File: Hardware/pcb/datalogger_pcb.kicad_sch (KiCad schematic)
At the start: 50 parts, among them J1 Micro_SD_Card_Det2, J2 Switch OUT, SW1 SW_Wuerth_450301014042, SW2 SW_Push, U1 DS3231MZ, U2 SN74LVC2G00DCTR

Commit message: Corrected errors in PCB
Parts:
- added RpullupCS1: 10k, Resistor_SMD:R_0805_2012Metric_Pad1.20x1.40mm_HandSolder, symbol Device:R
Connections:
- net +3.3V: now also RpullupCS1.1
- net CS: now also RpullupCS1.2
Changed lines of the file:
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@@
 	)
 	(junction
+		(at 218.44 142.24)
+		(diameter 0)
+		(color 0 0 0 0)
+	)
+	(junction
 		(at 229.87 36.83)
 		(diameter 0)
@@
 	(wire
 		(pts
-			(xy 226.06 142.24) (xy 237.49 142.24)
+			(xy 210.82 142.24) (xy 218.44 142.24)
 		)
 		(stroke
@@
 	(wire
 		(pts
+			(xy 218.44 142.24) (xy 237.49 142.24)
+		)
+		(stroke
+			(width 0)
+			(type default)
+		)
+	)
+	(wire
+		(pts
 			(xy 224.79 100.33) (xy 224.79 105.41)
 		)
@@
 	(wire
 		(pts
+			(xy 218.44 132.08) (xy 218.44 133.35)
+		)
+		(stroke
+			(width 0)
+			(type default)
+		)
+	)
+	(wire
+		(pts
 			(xy 163.83 82.55) (xy 185.42 82.55)
 		)
@@
 	(wire
 		(pts
+			(xy 218.44 140.97) (xy 218.44 142.24)
+		)
+		(stroke
+			(width 0)
+			(type default)
+		)
+	)
+	(wire
+		(pts
 			(xy 226.06 162.56) (xy 232.41 162.56)
 		)
@@
 	)
 	(label "CS"
-		(at 226.06 142.24 0)
+		(at 210.82 142.24 0)
 		(effects
 			(font
@@
 		(on_board yes)
 		(dnp no)
-		(fields_autoplaced yes)
 		(property "Reference" "#PWR02"
 			(at 220.98 151.13 0)
@@
 		)
 		(property "Value" "+3.3V"
-			(at 220.98 142.24 0)
+			(at 216.916 146.304 0)
 			(effects
 				(font
@@
 	)
 	(symbol
+		(lib_id "Device:R")
+		(at 218.44 137.16 0)
+		(unit 1)
+		(exclude_from_sim no)
+		(in_bom yes)
+		(on_board yes)
+		(dnp no)
+		(fields_autoplaced yes)
+		(property "Reference" "RpullupCS1"
+			(at 220.98 135.8899 0)
+			(effects
+				(font
+					(size 1.27 1.27)
+				)
+				(justify left)
+			)
+		)
+		(property "Value" "10k"
+			(at 220.98 138.4299 0)
+			(effects
+				(font
+					(size 1.27 1.27)
+				)
+				(justify left)
+			)
+		)
+		(property "Footprint" "Resistor_SMD:R_0805_2012Metric_Pad1.20x1.40mm_HandSolder"
+			(at 216.662 137.16 90)
+			(effects
+				(font
+					(size 1.27 1.27)
+				)
+				(hide yes)
+			)
+		)
+		(property "Datasheet" "~"
+			(at 218.44 137.16 0)
+			(effects
+				(font
+					(size 1.27 1.27)
+				)
+				(hide yes)
+			)
+		)
+		(property "Description" "Resistor"
+			(at 218.44 137.16 0)
+			(effects
+				(font
+					(size 1.27 1.27)
+				)
+				(hide yes)
+			)
+		)
+		(pin "1"
+		)
+		(pin "2"
+		)
+		(instances
+			(project "datalogger_pcb"
+				(path "/0cb0c659-ad14-4dc3-8b7e-e8b9c3c06858"
+					(reference "RpullupCS1")
+					(unit 1)
+				)
+			)
+		)
+	)
+	(symbol
 		(lib_id "power:+3.3V")
 		(at 76.2 151.13 0)
@@
 					(unit 1)
 				)
+			)
+		)
+	)
+	(symbol
+		(lib_id "power:+3.3V")
+		(at 218.44 132.08 0)
+		(unit 1)
+		(exclude_from_sim no)
+		(in_bom yes)
+		(on_board yes)
+		(dnp no)
+		(property "Reference" "#PWR024"
+			(at 218.44 135.89 0)
+			(effects
+				(font
+					(size 1.27 1.27)
+				)
+				(hide yes)
+			)
+		)
+		(property "Value" "+3.3V"
+			(at 222.504 130.556 0)
+			(effects
+				(font
+					(size 1.27 1.27)
+				)
+			)
+		)
+		(property "Footprint" ""
+			(at 218.44 132.08 0)
+			(effects
+				(font
+					(size 1.27 1.27)
+				)
+				(hide yes)
+			)
+		)
+		(property "Datasheet" ""
+			(at 218.44 132.08 0)
+			(effects
+				(font
+					(size 1.27 1.27)
+				)
+				(hide yes)
+			)
+		)
+		(property "Description" "Power symbol creates a global label with name \"+3.3V\""
+			(at 218.44 132.08 0)
+			(effects
+				(font
+					(size 1.27 1.27)
+				)
+				(hide yes)
+			)
+		)
+		(pin "1"
+		)
+		(instances
+			(project "datalogger_pcb"
+				(path "/0cb0c659-ad14-4dc3-8b7e-e8b9c3c06858"
+					(reference "#PWR024")
+					(unit 1)
+				)

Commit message: Improvements to PCB
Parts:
- removed MOSFET_12V1, MOSFET_5V1: BS170, Package_TO_SOT_THT:TO-92_Inline, symbol Transistor_FET:BS170
- removed R8: 100, Resistor_SMD:R_0805_2012Metric_Pad1.20x1.40mm_HandSolder, symbol Device:R
- removed R_pdown_MFET_1, R_pdown_MFET_2: 10k, Resistor_SMD:R_0805_2012Metric_Pad1.20x1.40mm_HandSolder, symbol Device:R
- added 12VSWTCH1, 5VSWTCH1: TPS22810DBV, Package_TO_SOT_SMD:SOT-23-6, symbol Power_Management:TPS22810DBV
- added C5, C6: 1uF, Capacitor_SMD:C_1812_4532Metric_Pad1.57x3.40mm_HandSolder, symbol Device:C
- added R6: 10k, Resistor_SMD:R_0805_2012Metric_Pad1.20x1.40mm_HandSolder, symbol Device:R
- R7: value 100 -> 10k
- R_BYPASS1: footprint Resistor_THT:R_Axial_DIN0204_L3.6mm_D1.6mm_P5.08mm_Vertical -> Resistor_SMD:R_0805_2012Metric_Pad1.20x1.40mm_HandSolder
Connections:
- net +12V: now also 12VSWTCH1.1 (VIN), C5.2
- net +5V: now also P_MOSFET1.3 (D), U2.8 (VCC)
- net +5VP: now also R_BYPASS1.2, 5VSWTCH1.1 (VIN), C6.2
- net GND: now also R7.2, 12VSWTCH1.2 (GND), 5VSWTCH1.2 (GND), C5.1, C6.1, R6.2
- net at J2.1 (Pin_1): now also 12VSWTCH1.5 (QOD), 12VSWTCH1.6 (VOUT)
- net at J2.2 (Pin_2): now also 5VSWTCH1.5 (QOD), 5VSWTCH1.6 (VOUT)
- net at A1.34 (GPIO28_ADC2), R7.1: now also 12VSWTCH1.3 (EN/UVLO)
- net at A1.19 (GPIO14), GPIO14-1.2 (Pin_2): now also 5VSWTCH1.3 (EN/UVLO), R6.1
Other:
- moved on the sheet: C3, J1, J2, R3, R4, R_BYPASS1, RpullupCS1

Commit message: Small changes
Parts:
- removed RpullupSCL0, RpullupSDA0: 10k, Resistor_THT:R_Axial_DIN0204_L3.6mm_D1.6mm_P5.08mm_Vertical, symbol Device:R

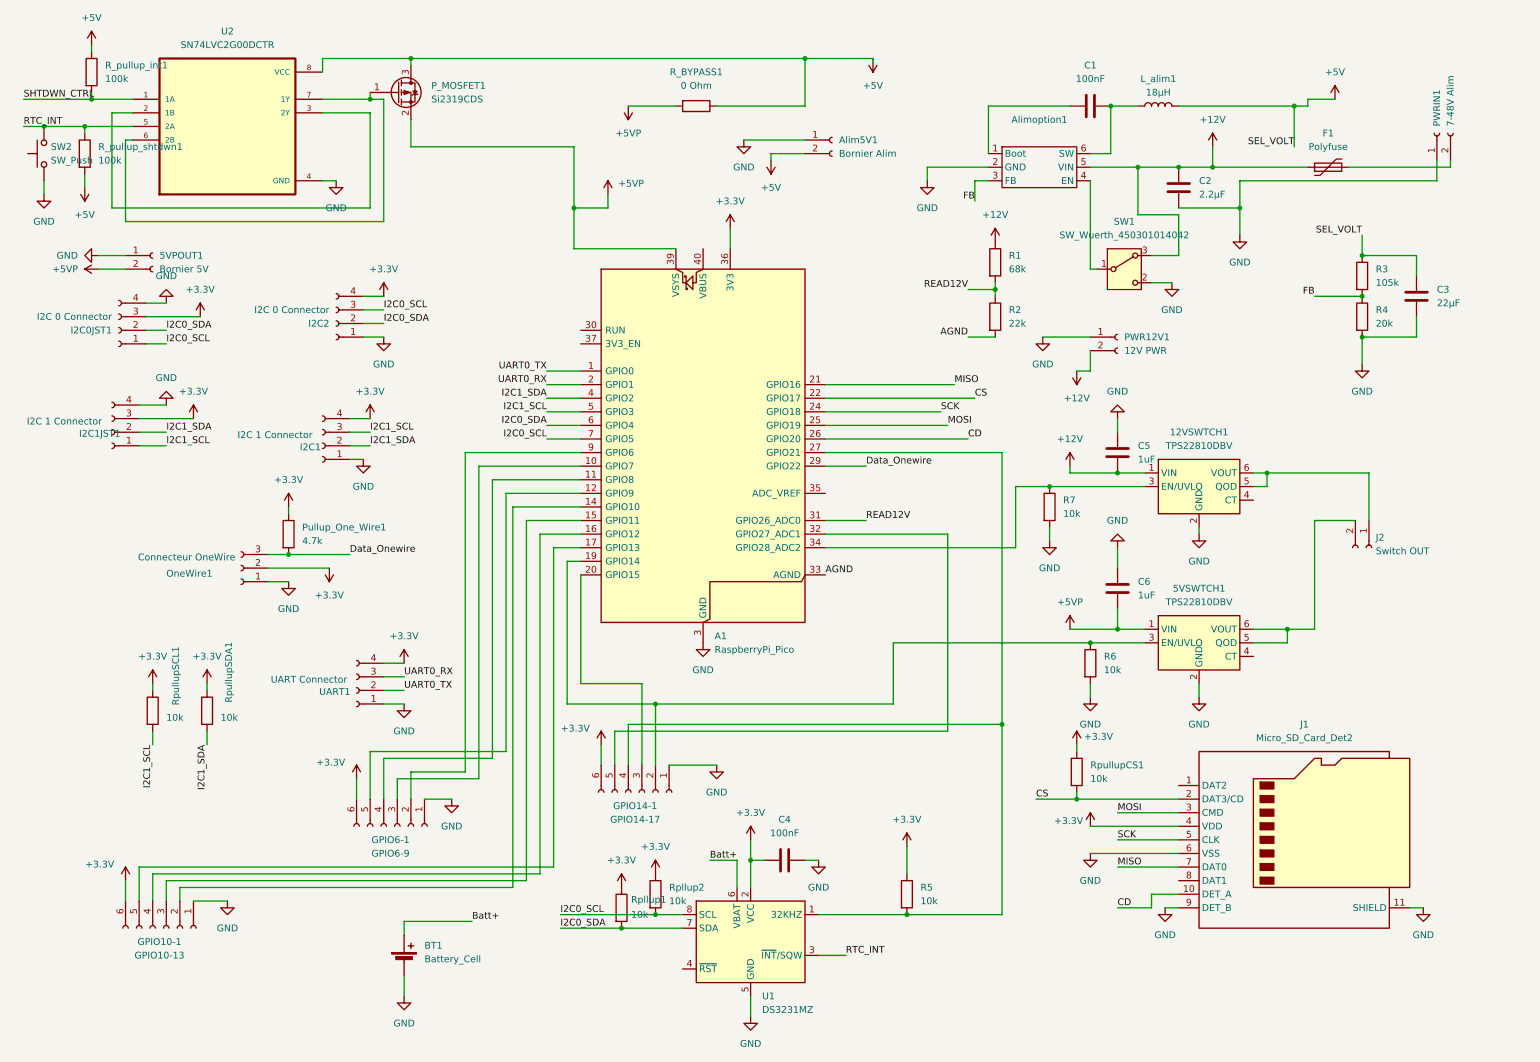
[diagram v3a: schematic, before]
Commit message: Improved datalogger design and reduced pcb size
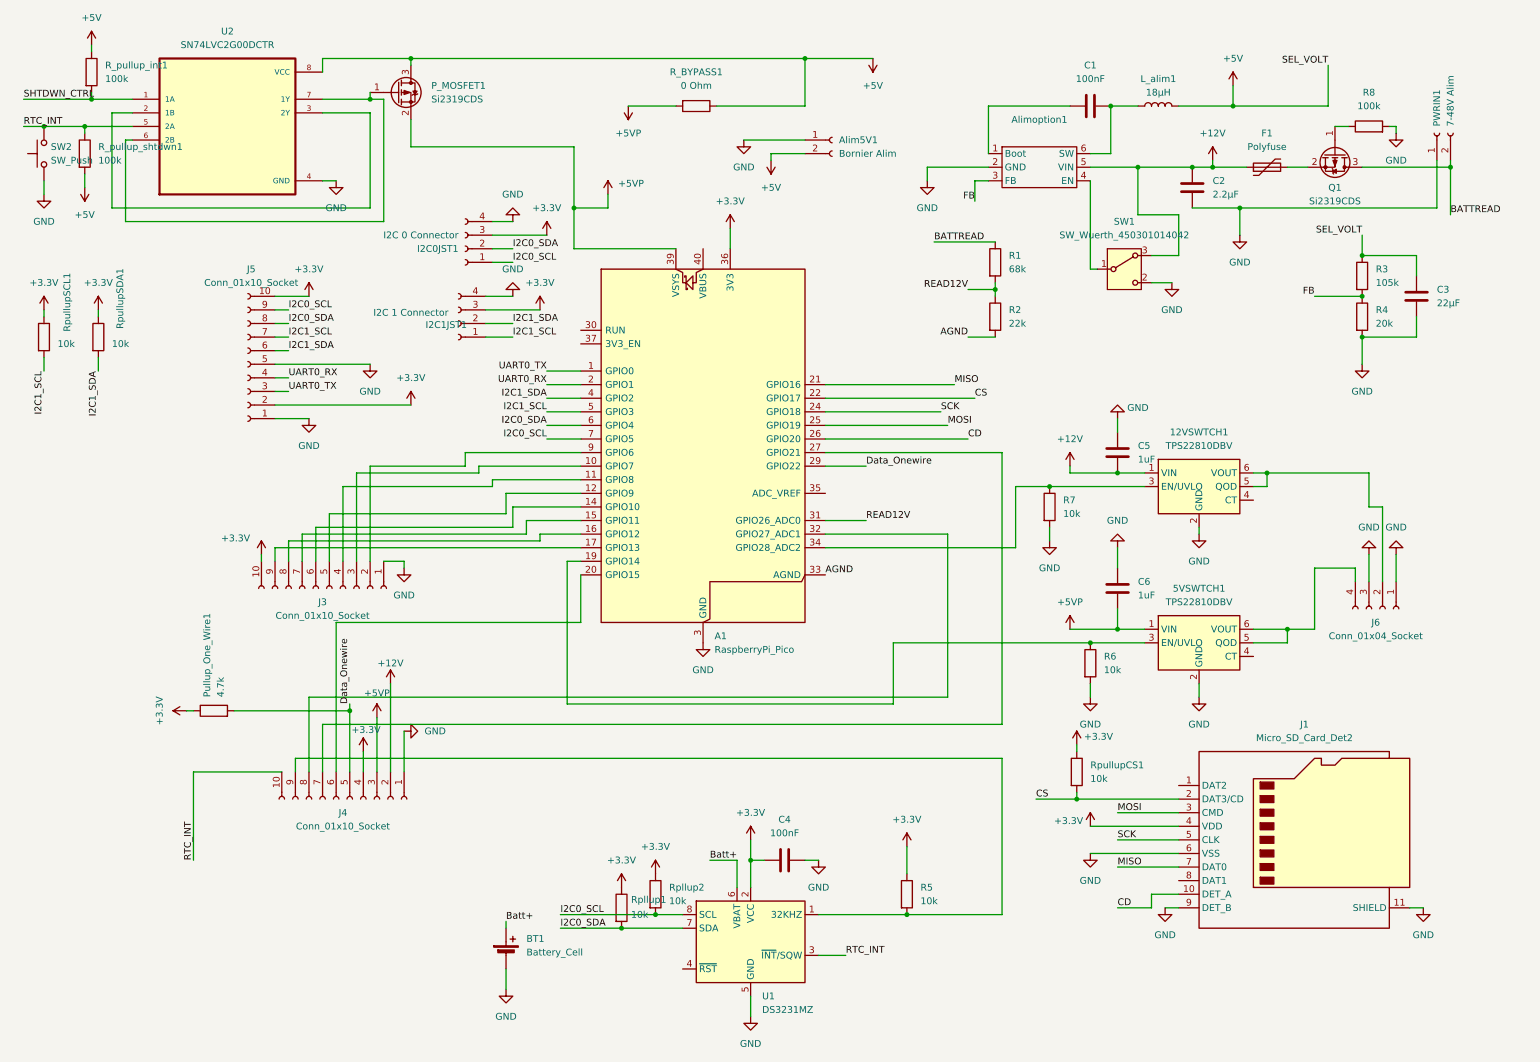
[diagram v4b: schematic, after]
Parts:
- removed 5VPOUT1: Bornier 5V, TerminalBlock_Phoenix:TerminalBlock_Phoenix_MKDS-1,5-2-5.08_1x02_P5.08mm_Horizontal, symbol Connector:Conn_01x02_Socket
- removed GPIO10-1: GPIO10-13, TerminalBlock_Phoenix:TerminalBlock_Phoenix_MKDS-1,5-6-5.08_1x06_P5.08mm_Horizontal, symbol Connector:Conn_01x06_Socket
- removed GPIO14-1: GPIO14-17, TerminalBlock_Phoenix:TerminalBlock_Phoenix_MKDS-1,5-6-5.08_1x06_P5.08mm_Horizontal, symbol Connector:Conn_01x06_Socket
- removed GPIO6-1: GPIO6-9, TerminalBlock_Phoenix:TerminalBlock_Phoenix_MKDS-1,5-6-5.08_1x06_P5.08mm_Horizontal, symbol Connector:Conn_01x06_Socket
- removed I2C1: I2C 1 Connector, TerminalBlock_Phoenix:TerminalBlock_Phoenix_MKDS-1,5-4-5.08_1x04_P5.08mm_Horizontal, symbol Connector:Conn_01x04_Socket
- removed I2C2: I2C 0 Connector, TerminalBlock_Phoenix:TerminalBlock_Phoenix_MKDS-1,5-4-5.08_1x04_P5.08mm_Horizontal, symbol Connector:Conn_01x04_Socket
- removed J2: Switch OUT, TerminalBlock_Phoenix:TerminalBlock_Phoenix_MKDS-1,5-2-5.08_1x02_P5.08mm_Horizontal, symbol Connector:Conn_01x02_Socket
- removed OneWire1: Connecteur OneWire, TerminalBlock_Phoenix:TerminalBlock_Phoenix_MKDS-1,5-3-5.08_1x03_P5.08mm_Horizontal, symbol Connector:Conn_01x03_Socket
- removed PWR12V1: 12V PWR, TerminalBlock_Phoenix:TerminalBlock_Phoenix_MKDS-1,5-2-5.08_1x02_P5.08mm_Horizontal, symbol Connector:Conn_01x02_Socket
- removed UART1: UART Connector, TerminalBlock_Phoenix:TerminalBlock_Phoenix_MKDS-1,5-4-5.08_1x04_P5.08mm_Horizontal, symbol Connector:Conn_01x04_Socket
- added J3, J4, J5: Conn_01x10_Socket, TerminalBlock_Phoenix:TerminalBlock_Phoenix_MKDS-1-10-3.81_1x10_P3.81mm_Horizontal, symbol Connector:Conn_01x10_Socket
- added J6: Conn_01x04_Socket, TerminalBlock_Phoenix:TerminalBlock_Phoenix_MKDS-1,5-4-5.08_1x04_P5.08mm_Horizontal, symbol Connector:Conn_01x04_Socket
- added Q1: Si2319CDS, Package_TO_SOT_SMD:SOT-23, symbol Transistor_FET:Si2319CDS
- added R8: 100k, Resistor_SMD:R_0805_2012Metric_Pad1.20x1.40mm_HandSolder, symbol Device:R
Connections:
- net +12V: now also J4.2 (Pin_2); no longer R1.1
- net +3.3V: now also J3.10 (Pin_10), J4.4 (Pin_4), J5.10 (Pin_10), J5.2 (Pin_2)
- net +5VP: now also J4.3 (Pin_3)
- net Data_Onewire: now also J4.5 (Pin_5)
- net GND: now also J3.1 (Pin_1), J4.1 (Pin_1), J5.1 (Pin_1), J5.5 (Pin_5), J6.1 (Pin_1), J6.3 (Pin_3), R8.2
- net I2C0_SCL: now also J5.9 (Pin_9)
- net I2C0_SDA: now also J5.8 (Pin_8)
- net I2C1_SCL: now also J5.7 (Pin_7)
- net I2C1_SDA: now also J5.6 (Pin_6)
- net RTC_INT: now also J4.10 (Pin_10)
- net UART0_RX: now also J5.4 (Pin_4)
- net UART0_TX: now also J5.3 (Pin_3)
- net at 12VSWTCH1.5 (QOD), 12VSWTCH1.6 (VOUT): now also J6.2 (Pin_2)
- net at 5VSWTCH1.5 (QOD), 5VSWTCH1.6 (VOUT): now also J6.4 (Pin_4)
- net at R5.2, U1.1 (32KHZ): now also J4.9 (Pin_9); no longer A1.27 (GPIO21)
- net at F1.2: now also Q1.2 (S); no longer PWRIN1.2 (Pin_2)
- net at A1.10 (GPIO7): now also J3.3 (Pin_3)
- net at A1.11 (GPIO8): now also J3.4 (Pin_4)
- net at A1.12 (GPIO9): now also J3.5 (Pin_5)
- net at A1.14 (GPIO10): now also J3.6 (Pin_6)
- net at A1.15 (GPIO11): now also J3.7 (Pin_7)
- net at A1.16 (GPIO12): now also J3.8 (Pin_8)
- net at A1.17 (GPIO13): now also J3.9 (Pin_9)
- net at A1.20 (GPIO15): now also J4.6 (Pin_6)
- net at A1.32 (GPIO27_ADC1): now also J4.8 (Pin_8)
- net at A1.9 (GPIO6): now also J3.2 (Pin_2)
- new net: A1.27 (GPIO21), J4.7 (Pin_7)
- new net: Q1.1 (G), R8.1
- new net BATTREAD: PWRIN1.2 (Pin_2), Q1.3 (D), R1.1
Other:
- moved on the sheet: BT1, C2, F1, I2C0JST1, I2C1JST1, Pullup_One_Wire1, RpullupSCL1, RpullupSDA1

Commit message: Changes to small pcb
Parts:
- removed P_MOSFET1: Si2319CDS, Package_TO_SOT_SMD:SOT-23, symbol Transistor_FET:Si2319CDS
- removed R_BYPASS1: 0 Ohm, Resistor_SMD:R_0805_2012Metric_Pad1.20x1.40mm_HandSolder, symbol Device:R
- removed R_pullup_int1, R_pullup_shtdwn1: 100k, Resistor_SMD:R_0805_2012Metric_Pad1.20x1.40mm_HandSolder, symbol Device:R
- removed SW2: SW_Push, Button_Switch_THT:SW_PUSH_6mm_H4.3mm, symbol Switch:SW_Push
- removed U2: SN74LVC2G00DCTR, nand:SSOP-8_2.95x2.8mm_P0.65mm - SN74LVC2G00, symbol SN74LVC2G00DCTR:SN74LVC2G00DCTR
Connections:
- net +5VP is gone; now on net +5V: 5VSWTCH1.1 (VIN), A1.39 (VSYS), C6.2, J4.3 (Pin_3)
